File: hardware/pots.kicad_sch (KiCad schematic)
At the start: 3 parts

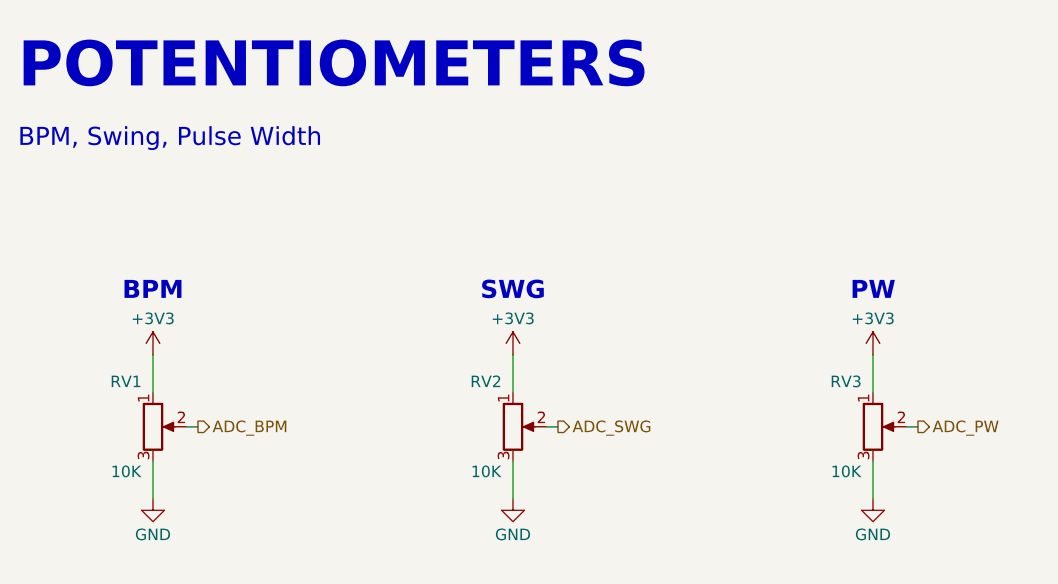
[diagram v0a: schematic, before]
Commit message: Complete hierarchical schematic sheets and fix wiring
- Complete encoder_leds sheet with MAX7219 + 64 LEDs
- Complete ui_leds sheet with MAX7219 + 45 LEDs
- Complete buttons sheet with MCP23017 + 40 buttons
- Complete display sheet with OLED I2C connector
- Complete pots sheet with 3 potentiometers
- Complete encoders sheet with 8 rotary encoders on MCP23017
- Fix inputs sheet hierarchical labels (CLK_IN, RST_IN, SCENE_CV_IN)
- Update MCU sheet with ADC hierarchical labels
- Update root sheet with hierarchical pin connections
- Various ERC fixes and wiring corrections

Co-Authored-By: Claude Opus 4.5 <noreply@anthropic.com>
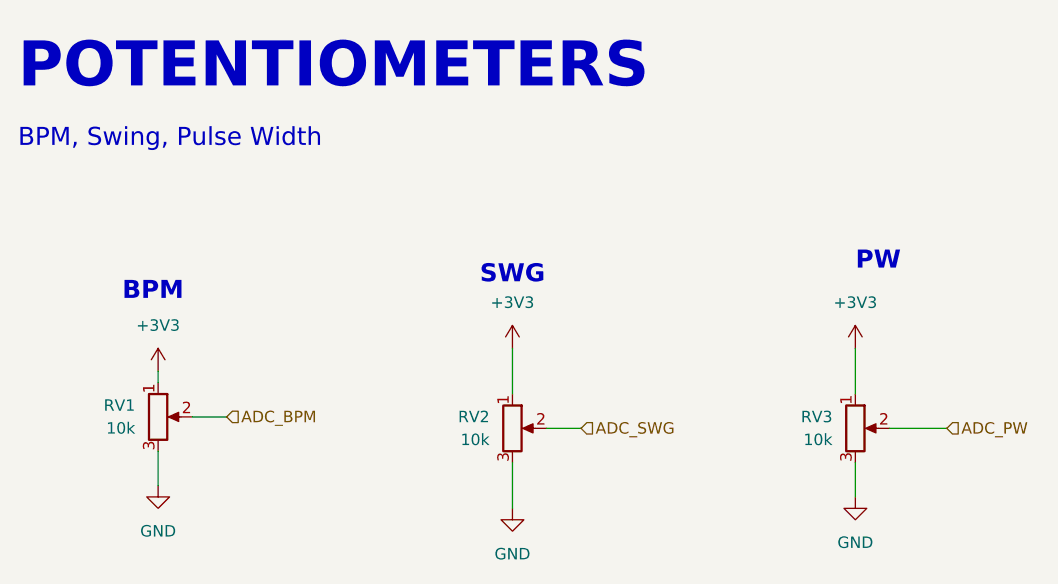
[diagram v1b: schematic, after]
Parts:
- removed RV1, RV2, RV3: 10K, symbol Device:R_POT
- added RV1, RV2, RV3: 10k, symbol Device:R_Potentiometer
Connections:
- net +3V3: now also RV1.1, RV2.1, RV3.1
- net ADC_BPM: now also RV1.2
- net ADC_PW: now also RV3.2
- net ADC_SWG: now also RV2.2
- net GND: now also RV1.3, RV2.3, RV3.3

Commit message: Assign footprints to all schematic components
SMD footprints assigned:
- Capacitors: 0402 (20pF), 0603 (100nF), 0805 (10uF), 1206 (47uF, 100uF)
- Resistors: 0603
- LEDs: 0201
- MAX7219: SOIC-24W
- ULN2003: SOIC-16
- Switches: TL3342 tactile
- Connectors: JST PH, pin headers

Also removes accidentally committed autosave files.

Co-Authored-By: Claude Opus 4.5 <noreply@anthropic.com>
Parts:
- RV1, RV2, RV3: footprint (none) -> Potentiometer_SMD:Potentiometer_ACP_CA6-VSMD_Vertical
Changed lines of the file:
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@@
 			)
 		)
-		(property "Footprint" ""
+		(property "Footprint" "Potentiometer_SMD:Potentiometer_ACP_CA6-VSMD_Vertical"
 			(at 115.57 88.9 0)
 			(effects
@@
 			)
 		)
-		(property "Footprint" ""
+		(property "Footprint" "Potentiometer_SMD:Potentiometer_ACP_CA6-VSMD_Vertical"
 			(at 193.04 90.17 0)
 			(effects
@@
 			)
 		)
-		(property "Footprint" ""
+		(property "Footprint" "Potentiometer_SMD:Potentiometer_ACP_CA6-VSMD_Vertical"
 			(at 154.94 90.17 0)
 			(effects
